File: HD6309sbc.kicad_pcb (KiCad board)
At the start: 2 copper layers, 99.8 x 99.8 mm, 32 parts, among them J1 Conn_01x02_Male, J2 Conn_02x30_Odd_Even, J3 Conn_01x02_Male, J4 Conn_01x06_Socket, J5 Conn_01x06_Socket, U1 HD63C09, U10 74LS375D, U11 74HC02, U12 74AHC1G08, U13 74HC21D, U14 74HC21D, U15 74HC21D, U4 UM61256FK, U5 74HC08, U6 28C256, U7 74HC04D, U8 74HC00D, U9 74LS375D

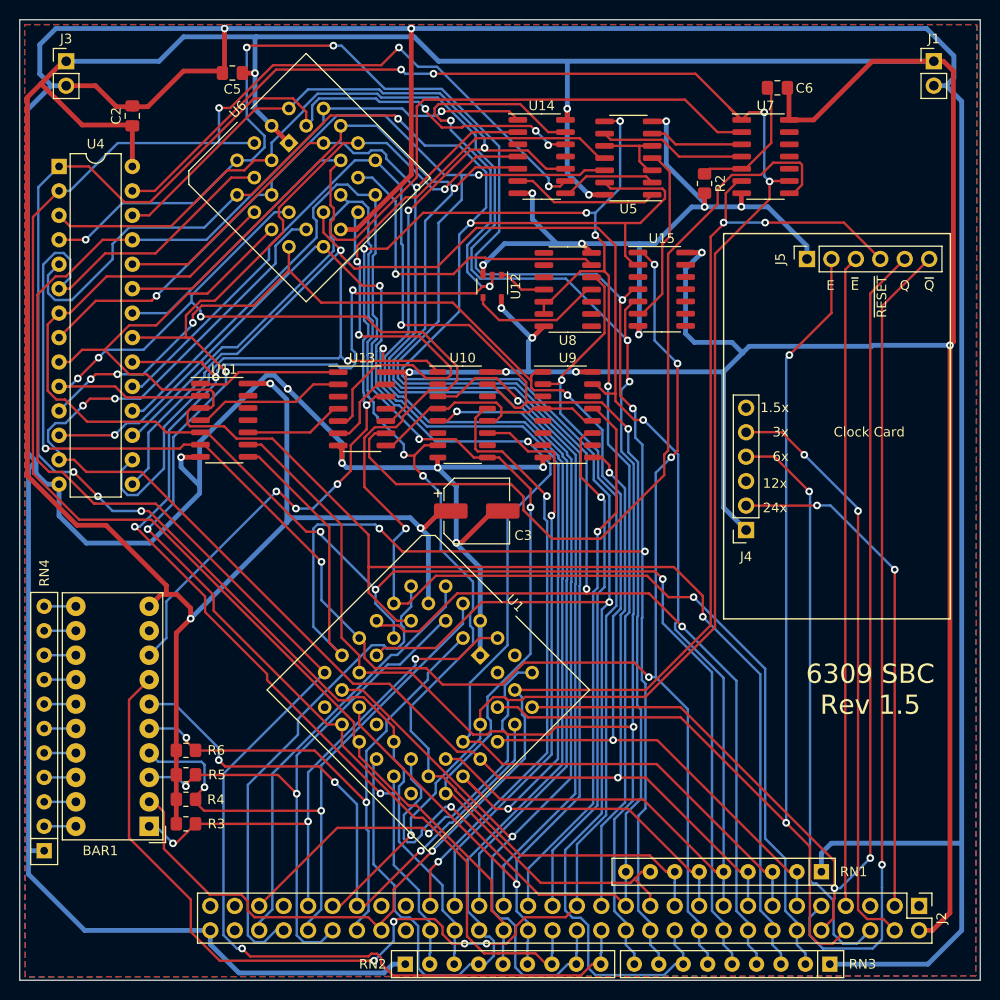
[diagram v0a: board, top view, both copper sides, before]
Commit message: fix rom footprint
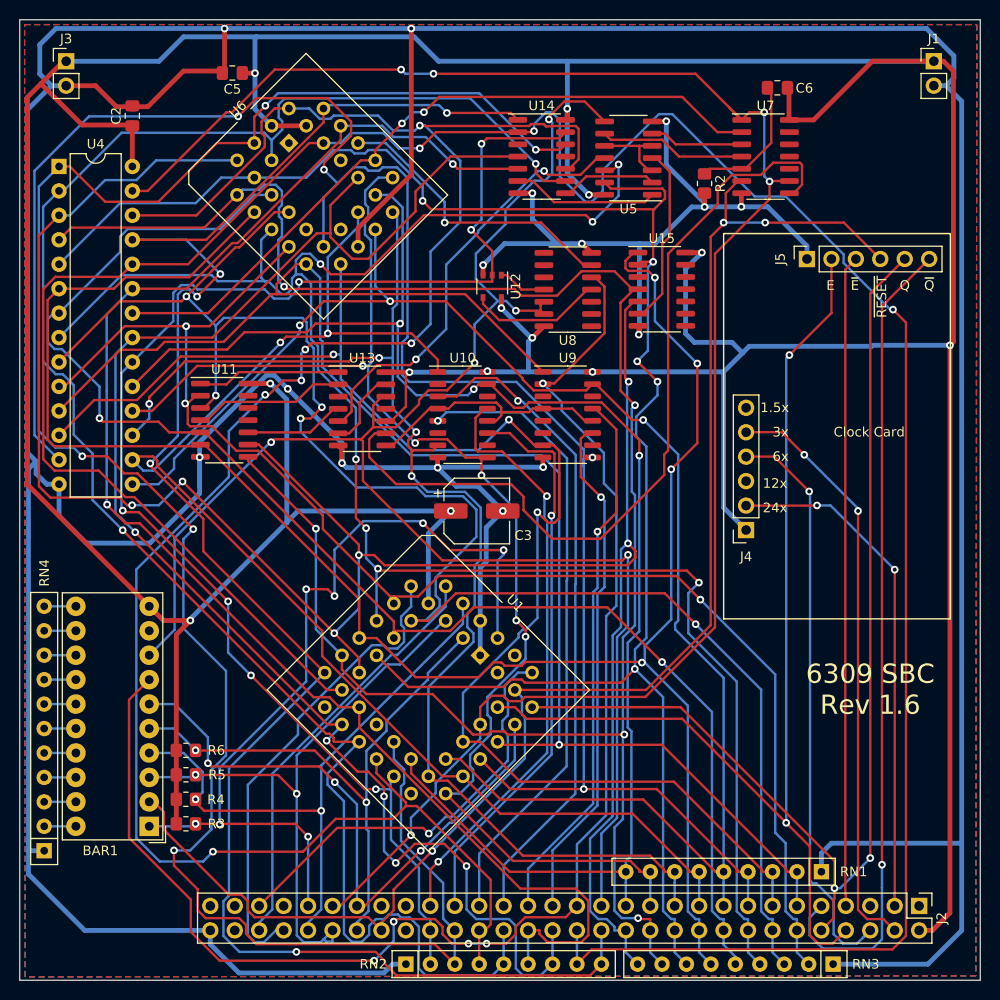
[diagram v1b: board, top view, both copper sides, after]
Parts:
- U6: footprint Package_LCC:PLCC-28_THT-Socket -> Package_LCC:PLCC-32_THT-Socket
- moved RN3 0.34 mm to (109.9, 123.5)
- moved RN2 0.07 mm to (65.5, 123.5)
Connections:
- U6 pad 1: +5V -> unconnected-(U6-DC-Pad1)
- U6 pad 10: A0 -> A1
- U6 pad 11: D0 -> A0
- U6 pad 12: D1 -> unconnected-(U6-NC-Pad12)
- U6 pad 13: D2 -> D0
- U6 pad 14: GND -> D1
- U6 pad 15: D3 -> D2
- U6 pad 16: D4 -> GND
- U6 pad 17: D5 -> unconnected-(U6-DC-Pad17)
- U6 pad 18: D6 -> D3
- U6 pad 19: D7 -> D4
- U6 pad 2: A12 -> A14
- U6 pad 20: Net-(U6-~{CE}) -> D5
- U6 pad 21: A10 -> D6
- U6 pad 22: ~{OE} -> D7
- U6 pad 23: A11 -> ~{OE}
- U6 pad 24: A9 -> A10
- U6 pad 25: A8 -> Net-(U6-~{OE})
- U6 pad 26: A13 -> unconnected-(U6-NC-Pad26)
- U6 pad 27: A14 -> A11
- U6 pad 28: +5V -> A9
- U6 pad 3: A7 -> A12
- U6 pad 4: A6 -> A7
- U6 pad 5: A5 -> A6
- U6 pad 6: A4 -> A5
- U6 pad 7: A3 -> A4
- U6 pad 8: A2 -> A3
- U6 pad 9: A1 -> A2
- U8 pad 6: Net-(U6-~{CE}) -> Net-(U6-~{OE})
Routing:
- net A9: track 186.2 -> 282.1 mm, vias 2 -> 3
- net A5: track 240.8 -> 194.7 mm, vias 3 -> 5
- net A14: track 172.6 -> 213.4 mm, vias 6 -> 5
- net D2: track 168.5 -> 208.4 mm
- net A0: track 187.9 -> 149.0 mm, vias 5 -> 3
- net A6: track 246.7 -> 210.8 mm, vias 7 -> 5
- net Net-(U6-~{CE}): track 33.9 -> 0.00 mm, vias 1 -> 0
- net ~{HALT}: track 57.9 -> 90.1 mm, vias 3 -> 7
- net Net-(U6-~{OE}): track 0.00 -> 30.8 mm, vias 0 -> 1
- net D4: track 161.9 -> 136.9 mm, vias 3 -> 2
- net Net-(U13-Pad5): track 69.2 -> 44.7 mm
- net D0: track 148.5 -> 172.9 mm, vias 5 -> 1
- net A11: track 178.2 -> 156.0 mm
- net A13: track 196.2 -> 216.6 mm, vias 2 -> 6
- net D7: track 178.3 -> 158.3 mm
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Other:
- board text added: "6309 SBC Rev 1.6"
- board text removed: "6309 SBC Rev 1.5"

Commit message: board refresh
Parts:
- added RN5: 470R, Resistor_THT:R_Array_SIP6, F.Cu at (27.9, 83.8)
- RN4: footprint Resistor_THT:R_Array_SIP11 -> Resistor_THT:R_Array_SIP6
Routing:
- net GND: track 587.3 -> 588.9 mm
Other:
- board text added: "6309 SBC Rev 1.7"
- board text removed: "6309 SBC Rev 1.6"

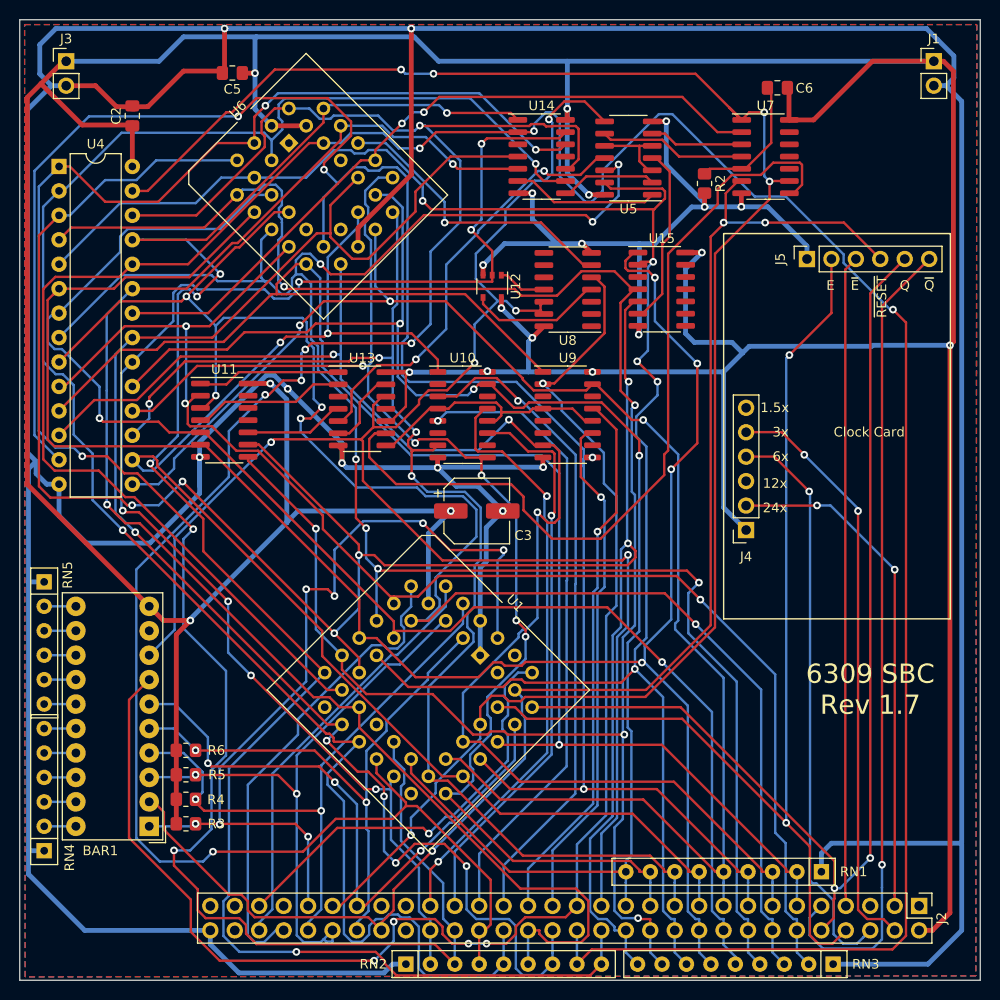
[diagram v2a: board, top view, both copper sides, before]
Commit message: Refine reset circuit
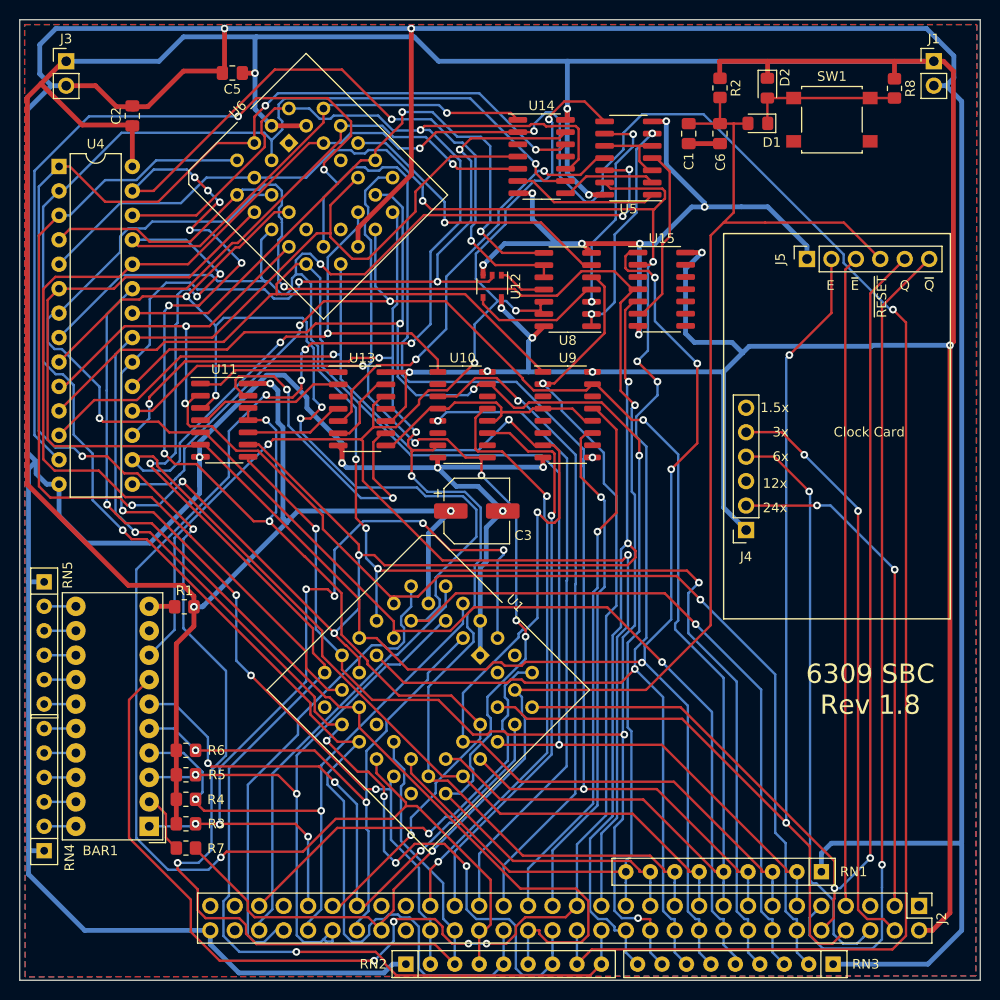
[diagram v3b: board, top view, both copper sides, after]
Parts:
- removed U7: 74HC04D, Package_SO:SOIC-14_3.9x8.7mm_P1.27mm
- added C1: 0.1uF, Capacitor_SMD:C_0805_2012Metric_Pad1.18x1.45mm_HandSolder, F.Cu at (94.9, 37.2)
- added D1: 1n4148, Diode_SMD:D_0805_2012Metric_Pad1.15x1.40mm_HandSolder, F.Cu at (102.1, 36.2)
- added D2: 1n4148, Diode_SMD:D_0805_2012Metric_Pad1.15x1.40mm_HandSolder, F.Cu at (103.1, 32.5)
- added R1: 1K, Resistor_SMD:R_0805_2012Metric_Pad1.20x1.40mm_HandSolder, F.Cu at (42.5, 86.4)
- added R7: 1K, Resistor_SMD:R_0805_2012Metric_Pad1.20x1.40mm_HandSolder, F.Cu at (42.7, 111.5)
- added R8: 100K, Resistor_SMD:R_0805_2012Metric_Pad1.20x1.40mm_HandSolder, F.Cu at (116.3, 32.5)
- added SW1: SW_Push, Button_Switch_SMD:SW_SPST_B3S-1000, F.Cu at (109.8, 35.8)
- R2: value 2.2K -> 100K
- moved R2 10.1 mm to (98.2, 32.5)
- moved C6 7.63 mm to (98.2, 37.2), turned to -90 degrees
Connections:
- BAR1 pad 10: +5V -> Net-(BAR1J-A)
- BAR1 pad 2: ~{RESET} -> Net-(BAR1B-A)
- C6 pad 1: +5V -> ~{RESET}
- C6 pad 2: Net-(C6-Pad2) -> GND
- R2 pad 1: Net-(C6-Pad2) -> +5V
- R2 pad 2: GND -> ~{RESET}
- U11 pad 11: unconnected-(U11-Pad11) -> R/~{W}
- U11 pad 12: unconnected-(U11-Pad12) -> R/~{W}
- U11 pad 13: unconnected-(U11-Pad13) -> Net-(U11-Pad13)
- U13 pad 9: Net-(U13-Pad9) -> Net-(U11-Pad13)
- U8 pad 1: unconnected-(U8-Pad1) -> Vector
- U8 pad 10: unconnected-(U8-Pad10) -> R/~{W}
- U8 pad 2: unconnected-(U8-Pad2) -> Vector
- U8 pad 3: unconnected-(U8-Pad3) -> Net-(U5-Pad9)
- U8 pad 8: unconnected-(U8-Pad8) -> ~{OE}
- U8 pad 9: unconnected-(U8-Pad9) -> R/~{W}
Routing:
- net Net-(U13-Pad9): track 87.4 -> 0.00 mm
- net Net-(U11-Pad13): track 0.00 -> 34.7 mm, vias 0 -> 2
- net Net-(D1-K): track 0.00 -> 15.9 mm
- net Net-(C6-Pad2): track 14.4 -> 0.00 mm
- net Vector: track 9.76 -> 23.3 mm, vias 0 -> 2
- net ~{OE}: track 74.8 -> 65.4 mm
- net R/~{W}: track 190.0 -> 198.3 mm, vias 5 -> 12
- net +5V: track 518.2 -> 525.8 mm
- net Net-(U5-Pad9): track 15.2 -> 22.2 mm, vias 0 -> 2
- net ~{RESET}: track 151.7 -> 158.1 mm, vias 3 -> 1
- net Net-(BAR1B-A): track 0.00 -> 6.25 mm
- net A15: track 149.5 -> 154.6 mm
- net Net-(BAR1J-A): track 0.00 -> 2.60 mm
- net A9: track 282.1 -> 284.1 mm
- net A2: track 198.4 -> 200.2 mm
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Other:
- board text added: "6309 SBC Rev 1.8"
- board text removed: "6309 SBC Rev 1.7"

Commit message: convert to new format
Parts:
- removed BAR1: HLCP-J100, Display:HLCP-J100
- removed RN4, RN5: 470R, Resistor_THT:R_Array_SIP6
- removed U10, U9: 74LS375D, Package_SO:SO-16_3.9x9.9mm_P1.27mm
- removed U11: 74HC02, Package_SO:SO-14_3.9x8.65mm_P1.27mm
- removed U13, U14, U15: 74HC21D, Package_SO:SOIC-14_3.9x8.7mm_P1.27mm
- removed U4: UM61256FK, Package_DIP:DIP-28_W7.62mm
- removed U5: 74HC08, Package_SO:SOIC-14_3.9x8.7mm_P1.27mm
- removed U6: 28C256, Package_LCC:PLCC-32_THT-Socket
- removed U8: 74HC00D, Package_SO:SOIC-14_3.9x8.7mm_P1.27mm
- added C4: 10uF, Capacitor_SMD:C_0805_2012Metric_Pad1.18x1.45mm_HandSolder, B.Cu at (43.0, 47.8)
- added C7: 10uF, Capacitor_SMD:C_0805_2012Metric_Pad1.18x1.45mm_HandSolder, B.Cu at (95.9, 106.7)
- added D10: LED_Filled, LED_SMD:LED_1206_3216Metric_Pad1.42x1.75mm_HandSolder, F.Cu at (47.1, 37.6)
- added D11: LED_Filled, LED_SMD:LED_1206_3216Metric_Pad1.42x1.75mm_HandSolder, F.Cu at (44.7, 37.6)
- added D12: LED_Filled, LED_SMD:LED_1206_3216Metric_Pad1.42x1.75mm_HandSolder, F.Cu at (37.4, 109.0)
- added D13: LED_Filled, LED_SMD:LED_1206_3216Metric_Pad1.42x1.75mm_HandSolder, F.Cu at (37.4, 106.6)
- added D14: LED_Filled, LED_SMD:LED_1206_3216Metric_Pad1.42x1.75mm_HandSolder, F.Cu at (37.4, 104.2)
- added D15: LED_Filled, LED_SMD:LED_1206_3216Metric_Pad1.42x1.75mm_HandSolder, F.Cu at (37.4, 101.8)
- added D16: LED_Filled, LED_SMD:LED_1206_3216Metric_Pad1.42x1.75mm_HandSolder, F.Cu at (37.4, 99.4)
- added D17: LED_Filled, LED_SMD:LED_1206_3216Metric_Pad1.42x1.75mm_HandSolder, F.Cu at (37.4, 97.0)
- added D3: GREEN, LED_SMD:LED_0805_2012Metric_Pad1.15x1.40mm_HandSolder, F.Cu at (104.1, 31.4)
- added D4: LED_Filled, LED_SMD:LED_1206_3216Metric_Pad1.42x1.75mm_HandSolder, F.Cu at (61.4, 37.6)
- added D5: LED_Filled, LED_SMD:LED_1206_3216Metric_Pad1.42x1.75mm_HandSolder, F.Cu at (59.1, 37.6)
- added D6: LED_Filled, LED_SMD:LED_1206_3216Metric_Pad1.42x1.75mm_HandSolder, F.Cu at (56.7, 37.6)
- added D7: LED_Filled, LED_SMD:LED_1206_3216Metric_Pad1.42x1.75mm_HandSolder, F.Cu at (54.3, 37.6)
- added D8: LED_Filled, LED_SMD:LED_1206_3216Metric_Pad1.42x1.75mm_HandSolder, F.Cu at (51.9, 37.6)
- added D9: LED_Filled, LED_SMD:LED_1206_3216Metric_Pad1.42x1.75mm_HandSolder, F.Cu at (49.5, 37.6)
- added R10: 470R, Resistor_SMD:R_0805_2012Metric_Pad1.20x1.40mm_HandSolder, B.Cu at (56.7, 33.5)
- added R11: 470R, Resistor_SMD:R_0805_2012Metric_Pad1.20x1.40mm_HandSolder, B.Cu at (54.3, 33.5)
- added R12: 470R, Resistor_SMD:R_0805_2012Metric_Pad1.20x1.40mm_HandSolder, B.Cu at (51.9, 33.5)
- added R13: 470R, Resistor_SMD:R_0805_2012Metric_Pad1.20x1.40mm_HandSolder, B.Cu at (49.5, 33.5)
- added R14: 470R, Resistor_SMD:R_0805_2012Metric_Pad1.20x1.40mm_HandSolder, B.Cu at (47.1, 33.5)
- added R15: 470R, Resistor_SMD:R_0805_2012Metric_Pad1.20x1.40mm_HandSolder, B.Cu at (44.7, 33.5)
- added R16: 470R, Resistor_SMD:R_0805_2012Metric_Pad1.20x1.40mm_HandSolder, B.Cu at (32.9, 109.1)
- added R17: 470R, Resistor_SMD:R_0805_2012Metric_Pad1.20x1.40mm_HandSolder, B.Cu at (32.9, 106.6)
- added R18: 470R, Resistor_SMD:R_0805_2012Metric_Pad1.20x1.40mm_HandSolder, B.Cu at (32.9, 104.2)
- added R19: 470R, Resistor_SMD:R_0805_2012Metric_Pad1.20x1.40mm_HandSolder, B.Cu at (32.9, 101.8)
- added R20: 470R, Resistor_SMD:R_0805_2012Metric_Pad1.20x1.40mm_HandSolder, B.Cu at (32.9, 99.3)
- added R21: 470R, Resistor_SMD:R_0805_2012Metric_Pad1.20x1.40mm_HandSolder, B.Cu at (32.9, 96.9)
- added R9: 330R, Resistor_SMD:R_0805_2012Metric_Pad1.20x1.40mm_HandSolder, F.Cu at (105.2, 34.4)
- added U16: 74HCT541, Package_SO:SOIC-20W_7.5x12.8mm_P1.27mm, F.Cu at (60.6, 53.6)
- added U17: 74HCT00, Package_SO:SOIC-14_3.9x8.7mm_P1.27mm, F.Cu at (39.9, 67.1)
- added U18: 74HCT04, Package_SO:SOIC-14_3.9x8.7mm_P1.27mm, F.Cu at (49.6, 67.1)
- added U19: 74HCT30, Package_SO:SOIC-14_3.9x8.7mm_P1.27mm, F.Cu at (90.9, 94.2)
- added U2: DS1813, Package_TO_SOT_SMD:SOT-23-3, B.Cu at (119.2, 37.2)
- added U3: 74AHC1G14, Package_TO_SOT_SMD:SOT-353_SC-70-5_Handsoldering, B.Cu at (113.7, 36.9)
- added U7: 74HCT574, Package_SO:SOIC-20W_7.5x12.8mm_P1.27mm, F.Cu at (40.9, 53.6)
- C1: value 0.1uF -> 10uF; moved to B.Cu
- C2, C5, C6: value 1uF -> 10uF; moved to B.Cu
- D1: value 1n4148 -> RED; footprint Diode_SMD:D_0805_2012Metric_Pad1.15x1.40mm_HandSolder -> LED_SMD:LED_0805_2012Metric_Pad1.15x1.40mm_HandSolder
- D2: value 1n4148 -> YELLOW; footprint Diode_SMD:D_0805_2012Metric_Pad1.15x1.40mm_HandSolder -> LED_SMD:LED_0805_2012Metric_Pad1.15x1.40mm_HandSolder
- J4, J5: value Conn_01x06_Socket -> Conn_01x07_Socket; footprint Connector_PinSocket_2.54mm:PinSocket_1x06_P2.54mm_Vertical -> Connector_PinSocket_2.54mm:PinSocket_1x07_P2.54mm_Vertical
- R1, R7: value 1K -> 470R; moved to B.Cu
- R2, R8: value 100K -> 330R
- U12: value 74AHC1G08 -> 74HCT138; footprint Package_SO:TSOP-5_1.65x3.05mm_P0.95mm -> Package_SO:SOIC-16_3.9x9.9mm_P1.27mm
- moved R7 79.7 mm to (59.1, 33.5), turned to 90 degrees
- moved C1 58.9 mm to (41.3, 61.5), turned to 180 degrees
- moved R1 56.2 mm to (61.4, 33.5), turned to 90 degrees
- moved U12 53.6 mm to (90.4, 104.3)
- moved C6 53.2 mm to (88.2, 89.5), turned to 0 degrees
- moved C2 29.5 mm to (51.0, 61.4), turned to 180 degrees
- moved C5 22.5 mm to (62.3, 47.8)
- moved R2 18.6 mm to (116.6, 34.4)
- moved D1 14.3 mm to (115.6, 31.3)
- moved SW1 7.88 mm to (116.0, 40.7)
- moved D2 6.91 mm to (109.9, 31.3), turned to 180 degrees
- moved R8 5.71 mm to (110.9, 34.5)
- moved J4 2.57 mm to (100.9, 81.0)
- moved J5 2.49 mm to (104.7, 50.3)
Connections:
- net A0 renamed /A0
- net A1 renamed /A1
- net A10 renamed /A10
- net A11 renamed /A11
- net A12 renamed /A12
- net A13 renamed /A13
- net A14 renamed /A14
- net A2 renamed /A2
- net A3 renamed /A3
- net A4 renamed /A4
- net A8 renamed /A8
- net A9 renamed /A9
- net D0 renamed /D0
- net D1 renamed /D1
- net D2 renamed /D2
- net D3 renamed /D3
- net D4 renamed /D4
- net D5 renamed /D5
- net D6 renamed /D6
- net D7 renamed /D7
- net MRDY renamed AVMA
- net ~{DMA} renamed BUSY
- C1 pad 1: ~{RESET} -> +5V
- C6 pad 1: ~{RESET} -> +5V
- D1 pad 2: ~{RESET} -> Net-(D1-A)
- D2 pad 1: +5V -> Net-(D2-K)
- D2 pad 2: Net-(D1-K) -> ~{RESET}
- J2 pad 22: A5 -> /A5
- J2 pad 24: A6 -> /A6
- J2 pad 26: A7 -> /A7
- J2 pad 27: MAPPED_MEM -> SELPA
- J2 pad 29: ROM/~{RAM} -> SELPB
- J2 pad 31: Q1 -> SELPC
- J2 pad 33: Q2 -> SELPD
- J2 pad 35: Q3 -> SELPE
- J2 pad 37: Q4 -> SELPF
- J2 pad 39: Q5 -> SELPG
- J2 pad 41: Q6 -> SELPH
- J2 pad 42: A15 -> /A15
- J2 pad 43: Q7 -> unconnected-(J2-Pin_43-Pad43)
- J2 pad 45: Q8 -> unconnected-(J2-Pin_45-Pad45)
- J2 pad 5: unconnected-(J2-Pin_5-Pad5) -> Clock12
- J4 pad 1: +5V -> /intD0
- J4 pad 2: Clock24 -> /intD1
- J4 pad 3: Clock12 -> Clock24
- J4 pad 4: Clock6 -> Clock12
- J4 pad 5: Clock3 -> Clock6
- J4 pad 6: Clock1.5 -> Clock3
- R1 pad 2: +5V -> GND
- R2 pad 1: +5V -> Net-(D1-K)
- R2 pad 2: ~{RESET} -> GND
- R7 pad 2: ~{RESET} -> GND
- R8 pad 1: +5V -> Net-(D2-K)
- R8 pad 2: Net-(D1-K) -> GND
- RN2 pad 2: A15 -> /A15
- RN3 pad 7: A5 -> /A5
- RN3 pad 8: A6 -> /A6
- RN3 pad 9: A7 -> /A7
- SW1 pad 1: Net-(D1-K) -> ~{RESET}
- U1 pad 14: A5 -> /A5
- U1 pad 15: A6 -> /A6
- U1 pad 16: A7 -> /A7
- U1 pad 26: A15 -> /A15
- U1 pad 42: unconnected-(U1-EXTAL-Pad42) -> LIC
- U1 pad 43: unconnected-(U1-XTAL-Pad43) -> TSC
- U12 pad 1: Net-(U12-Pad1) -> /A5
- U12 pad 2: A15 -> /A6
- U12 pad 3: GND -> /A7
- U12 pad 4: Net-(U12-Pad4) -> GND
- U12 pad 5: +5V -> /MemoryDecoder/MappedMem
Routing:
- net GND: track 590.0 -> 12.5 mm
- net +5V: track 525.8 -> 41.5 mm, vias 13 -> 10
- net A7: track 226.4 -> 0.00 mm, vias 6 -> 0
- net /A9: track 284.1 -> 70.5 mm, vias 3 -> 2
- net A6: track 211.9 -> 0.00 mm, vias 5 -> 0
- net A5: track 194.4 -> 0.00 mm, vias 5 -> 0
- net MAPPED_MEM: track 174.7 -> 0.00 mm, vias 5 -> 0
- net /A13: track 217.7 -> 59.1 mm, vias 6 -> 2
- net A15: track 154.6 -> 0.00 mm, vias 7 -> 0
- net /A14: track 213.4 -> 58.8 mm, vias 5 -> 1
- net ROM/~{RAM}: track 152.1 -> 0.00 mm, vias 5 -> 0
- net /A4: track 199.5 -> 54.8 mm, vias 4 -> 1
- net /A2: track 200.2 -> 63.8 mm, vias 7 -> 1
- net SELPD: track 0.00 -> 109.3 mm, vias 0 -> 4
- net /A12: track 190.0 -> 84.9 mm
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- added copper zone on In2.Cu, net +5V
- added copper zone on In1.Cu, net GND
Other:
- copper layers 2 -> 4
- board text added: "6309 SBC Rev 2.0"
- board text added: "6309e CPU Card"
- board text added: "GPR PD0"
- board text added: "PDA"
- board text added: "PDB"
- board text added: "PDC"
- board text added: "PDD"
- board text added: "PDE"
- board text added: "PDF"
- board text added: "PDG"
- board text added: "PDH"
- board text removed: "6309 SBC Rev 1.8"
